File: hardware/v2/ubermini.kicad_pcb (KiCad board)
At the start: 4 copper layers, 76.2 x 63.5 mm, 71 parts, among them J1 USB_OTG, P1 SMA-CONN, P2 sma, P3 sma, P4 uart1, P5 SWD, P6 boot, P7 sma, SW1 SW_PUSH, U1 CC2591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

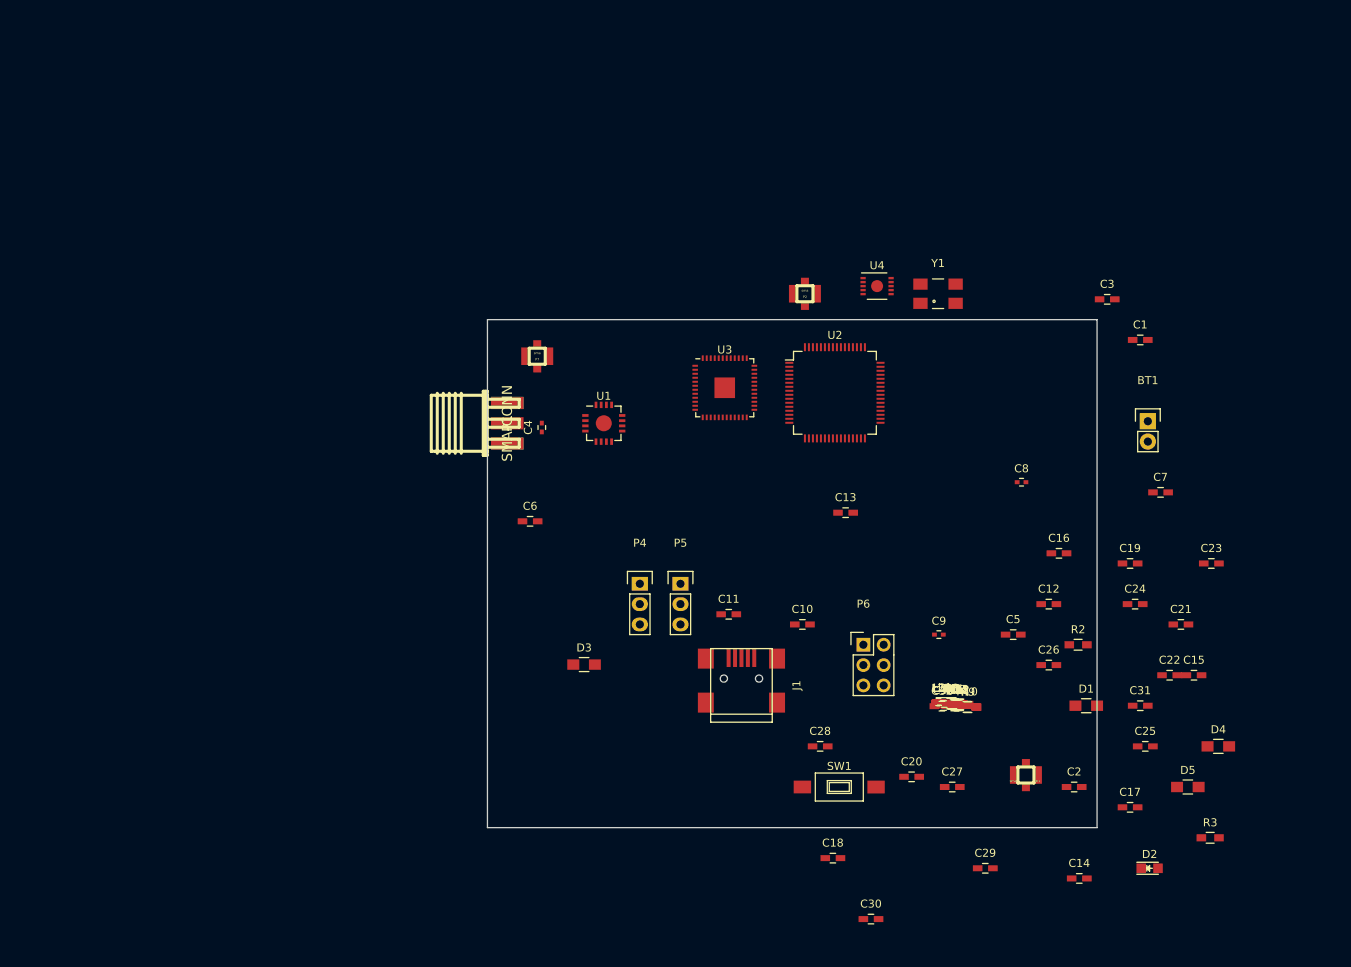
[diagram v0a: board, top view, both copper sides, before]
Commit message: hw v2 add pcb
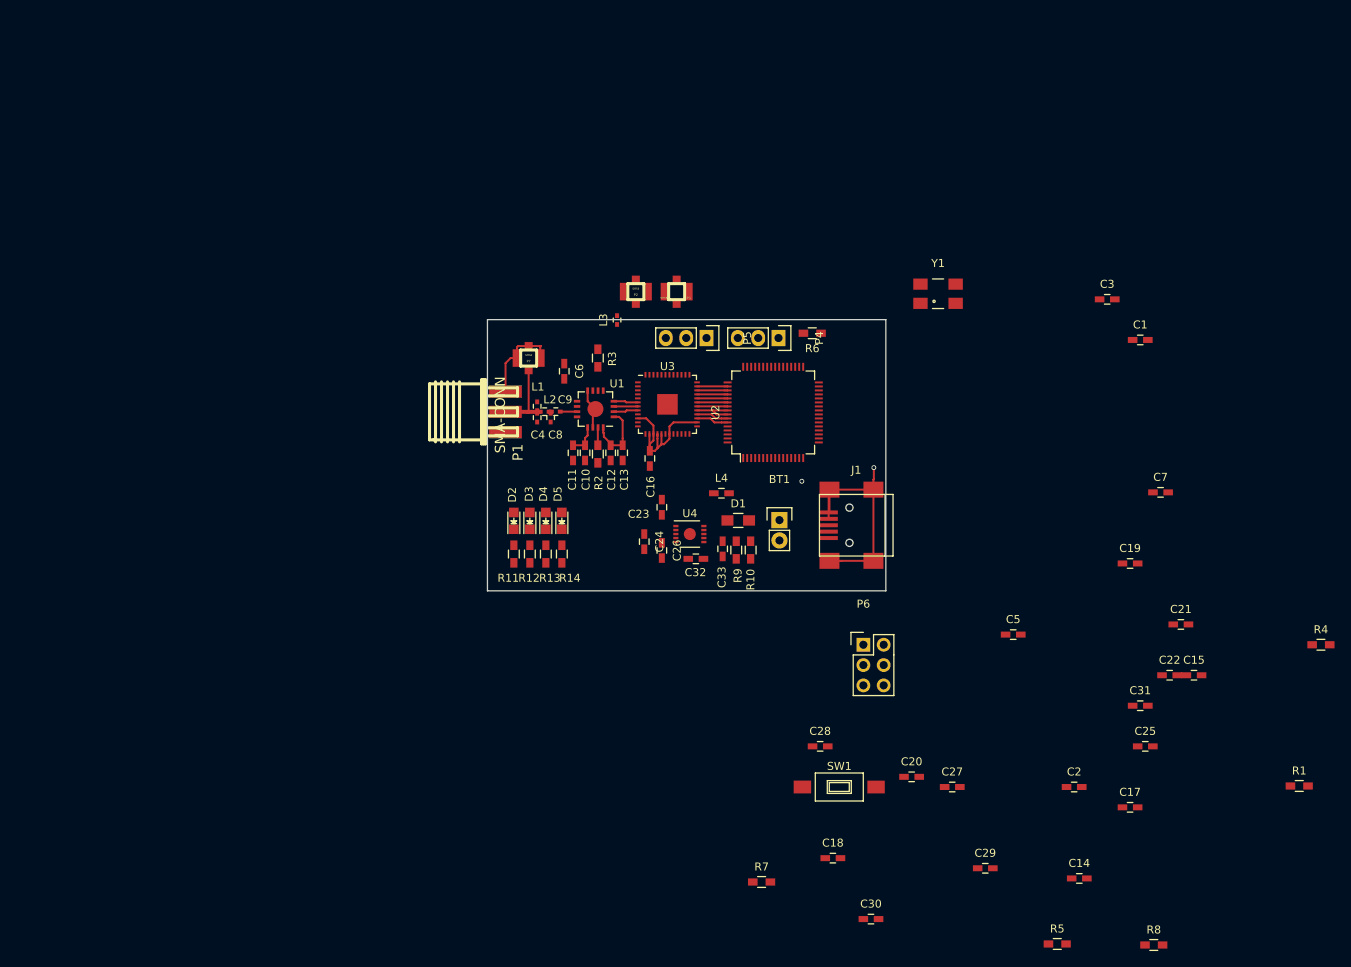
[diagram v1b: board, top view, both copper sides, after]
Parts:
- D3, D4, D5: footprint Resistors_SMD:R_0805_HandSoldering -> LEDs:LED_0805
- moved R3 97.2 mm to (128.1, 81.0), turned to 270 degrees
- moved D2 90.6 mm to (117.6, 101.3), turned to 90 degrees
- moved D4 88.7 mm to (121.6, 101.3), turned to 90 degrees
- moved D5 85.0 mm to (123.6, 101.3), turned to 90 degrees
- moved P3 74.5 mm to (138.0, 72.7)
- moved C23 69.0 mm to (136.1, 99.7), turned to 90 degrees
- moved R2 64.6 mm to (128.1, 93.0), turned to 270 degrees
- moved L3 62.4 mm to (130.5, 76.2), turned to 90 degrees
- moved L1 62.3 mm to (120.5, 87.0), turned to 270 degrees
- moved C24 61.9 mm to (133.9, 104.0), turned to 270 degrees
- moved L2 61.1 mm to (121.5, 87.7)
- moved C8 59.4 mm to (122.2, 88.5), turned to 90 degrees
- moved R11 58.0 mm to (117.6, 105.5), turned to 270 degrees
- moved C12 57.9 mm to (129.7, 92.8), turned to 270 degrees
- moved R12 56.9 mm to (119.6, 105.5), turned to 270 degrees
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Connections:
- U2 pad 50: (no net) -> /GIO6
- U2 pad 51: (no net) -> /SO
- U2 pad 52: (no net) -> /SI
- U2 pad 53: (no net) -> /SCLK
- U2 pad 54: (no net) -> /CSn
- U2 pad 55: (no net) -> /DCLK
- U2 pad 56: (no net) -> /DIO
- U2 pad 57: (no net) -> /DIO
- U2 pad 58: (no net) -> /TX
- U2 pad 59: (no net) -> /RX
- U3 pad 27: (no net) -> /RX
- U3 pad 28: (no net) -> /TX
- U3 pad 29: (no net) -> /DIO
- U3 pad 30: (no net) -> /DCLK
- U3 pad 31: (no net) -> /CSn
- U3 pad 32: (no net) -> /SCLK
- U3 pad 33: (no net) -> /SI
- U3 pad 34: (no net) -> /SO
- U3 pad 35: (no net) -> /GIO6
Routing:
- net GND: track 0.00 -> 55.5 mm, vias 0 -> 2
- net +1V8: track 0.00 -> 19.4 mm
- net +3.3VA: track 0.00 -> 12.4 mm
- net Net-(C4-Pad2): track 0.00 -> 10.4 mm
- net /DIO: track 0.00 -> 5.92 mm
- net /TX: track 0.00 -> 4.03 mm
- net /RX: track 0.00 -> 4.03 mm
- net /SO: track 0.00 -> 3.82 mm
- net /SI: track 0.00 -> 3.82 mm
- net /SCLK: track 0.00 -> 3.82 mm
- net /GIO6: track 0.00 -> 3.82 mm
- net /DCLK: track 0.00 -> 3.82 mm
- net /CSn: track 0.00 -> 3.82 mm
- net Net-(L3-Pad2): track 0.00 -> 3.07 mm
- net Net-(L3-Pad1): track 0.00 -> 3.06 mm
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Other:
- board size 76.2 x 63.5 mm -> 49.8 x 33.9 mm

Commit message: hw patch
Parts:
- moved R8 76.2 mm to (129.5, 120.2), turned to 180 degrees
- moved R1 71.4 mm to (147.9, 112.3)
- moved C18 70.1 mm to (130.6, 78.8), turned to 270 degrees
- moved C19 62.1 mm to (139.2, 78.8), turned to 90 degrees
- moved C1 59.5 mm to (148.1, 114.1), turned to 180 degrees
- moved R5 56.4 mm to (140.6, 120.2), turned to 180 degrees
- moved SW1 51.8 mm to (170.8, 84.4), turned to 90 degrees
- moved R7 49.9 mm to (156.9, 97.3), turned to 90 degrees
- moved Y1 36.2 mm to (134.9, 79.0)
- moved BT1 33.2 mm to (118.1, 106.8), turned to 180 degrees
- moved P6 31.9 mm to (159.0, 85.1)
- moved D2 23.4 mm to (141.0, 101.7)
- moved D3 23.4 mm to (143.0, 101.8)
- moved D4 23.4 mm to (145.0, 101.7)
- moved D5 23.4 mm to (147.0, 101.7)
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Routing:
- net GND: track 55.5 -> 5.30 mm, vias 2 -> 0
- net Net-(C4-Pad2): track 10.4 -> 5.18 mm

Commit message: hw update
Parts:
- C2, C22, C27, C28, C29, C30, C5, R3, R4, R8: moved to B.Cu
- moved C14 84.6 mm to (130.5, 84.2), turned to 180 degrees
- moved R4 84.6 mm to (140.4, 84.2), turned to 180 degrees
- moved C15 80.4 mm to (131.7, 82.9), turned to 180 degrees
- moved C7 75.0 mm to (124.6, 84.5), turned to 270 degrees
- moved C17 72.3 mm to (136.2, 94.5), turned to 270 degrees
- moved C29 65.4 mm to (146.2, 86.8), turned to 270 degrees
- moved C25 63.1 mm to (141.3, 99.0), turned to 270 degrees
- moved C21 62.4 mm to (142.1, 93.8), turned to 270 degrees
- moved C30 62.3 mm to (146.4, 90.8), turned to 90 degrees
- moved C31 61.9 mm to (139.5, 99.0), turned to 270 degrees
- moved C2 61.0 mm to (151.4, 85.5), turned to 180 degrees
- moved C20 57.5 mm to (140.3, 82.6), turned to 180 degrees
- moved C3 56.4 mm to (139.6, 95.0), turned to 90 degrees
- moved C22 55.8 mm to (151.9, 91.6), turned to 180 degrees
- moved C27 54.3 mm to (152.8, 84.0), turned to 180 degrees
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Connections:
- net /ATEST1 renamed /ATEST1_P
- net /ATEST2 renamed /ATEST2_N
- D2 pad 2: (no net) -> /LED1
- D3 pad 2: (no net) -> /LED2
- D4 pad 2: (no net) -> /LED3
- D5 pad 2: (no net) -> /LED4
- U1 pad 7: (no net) -> /HGM
- U2 pad 1: (no net) -> Net-(U2-Pad1)
- U2 pad 10: (no net) -> /LED3
- U2 pad 11: (no net) -> /LED4
- U2 pad 14: (no net) -> Net-(U2-Pad14)
- U2 pad 15: (no net) -> Net-(U2-Pad15)
- U2 pad 16: (no net) -> Net-(U2-Pad16)
- U2 pad 17: (no net) -> Net-(U2-Pad17)
- U2 pad 2: (no net) -> Net-(U2-Pad2)
- U2 pad 20: (no net) -> /SPI1_CS
- U2 pad 21: (no net) -> /SPI1_SCK
- U2 pad 22: (no net) -> /SPI1_MI
- U2 pad 23: (no net) -> /SPI1_MO
- U2 pad 24: (no net) -> Net-(U2-Pad24)
- U2 pad 25: (no net) -> Net-(U2-Pad25)
- U2 pad 26: (no net) -> Net-(U2-Pad26)
- U2 pad 27: (no net) -> Net-(U2-Pad27)
- U2 pad 29: (no net) -> Net-(U2-Pad29)
- U2 pad 3: (no net) -> Net-(U2-Pad3)
- U2 pad 30: (no net) -> Net-(U2-Pad30)
- U2 pad 33: (no net) -> Net-(U2-Pad33)
- U2 pad 34: (no net) -> Net-(U2-Pad34)
- U2 pad 35: (no net) -> Net-(U2-Pad35)
- U2 pad 36: (no net) -> Net-(U2-Pad36)
- U2 pad 37: (no net) -> Net-(U2-Pad37)
- U2 pad 38: (no net) -> Net-(U2-Pad38)
- U2 pad 39: (no net) -> Net-(U2-Pad39)
- U2 pad 4: (no net) -> Net-(U2-Pad4)
- U2 pad 40: (no net) -> Net-(U2-Pad40)
- U2 pad 41: (no net) -> Net-(U2-Pad41)
- U2 pad 6: (no net) -> Net-(U2-Pad6)
- U2 pad 61: (no net) -> /GR
- U2 pad 62: (no net) -> Net-(U2-Pad62)
- U2 pad 8: (no net) -> /LED1
- U2 pad 9: (no net) -> /LED2
- U3 pad 11: (no net) -> Net-(U3-Pad11)
- U3 pad 12: (no net) -> Net-(U3-Pad12)
- U3 pad 13: (no net) -> Net-(U3-Pad13)
- U3 pad 20: (no net) -> /GR
- U3 pad 36: (no net) -> Net-(U3-Pad36)
- U3 pad 37: (no net) -> Net-(U3-Pad37)
- U3 pad 38: (no net) -> Net-(U3-Pad38)
- U3 pad 39: (no net) -> Net-(U3-Pad39)
- U3 pad 40: (no net) -> Net-(U3-Pad40)
- U4 pad 2: (no net) -> Net-(U4-Pad2)
- U4 pad 7: +3.3VA -> Net-(C33-Pad2)
- U4 pad 9: (no net) -> Net-(U4-Pad9)
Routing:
- net GND: track 5.30 -> 227.9 mm, vias 0 -> 17
- net /VBUS: track 0.00 -> 50.1 mm, vias 0 -> 2
- net Net-(R7-Pad2): track 0.00 -> 19.6 mm, vias 0 -> 2
- net /ATEST1_P: track 0.00 -> 18.8 mm, vias 0 -> 2
- net /ATEST2_N: track 0.00 -> 18.7 mm, vias 0 -> 2
- net Net-(R6-Pad2): track 0.00 -> 18.2 mm
- net +1V8: track 19.4 -> 37.3 mm
- net /NRST: track 0.00 -> 17.0 mm, vias 0 -> 2
- net Net-(P6-Pad3): track 0.00 -> 13.9 mm
- net +3.3VA: track 12.4 -> 24.7 mm
- net /GR: track 0.00 -> 11.5 mm, vias 0 -> 2
- net +3V3: track 0.00 -> 10.5 mm, vias 0 -> 2
- net /BOOT0: track 0.00 -> 10.3 mm, vias 0 -> 1
- net Net-(C3-Pad1): track 0.00 -> 10.3 mm
- net Net-(C4-Pad2): track 5.18 -> 15.0 mm
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
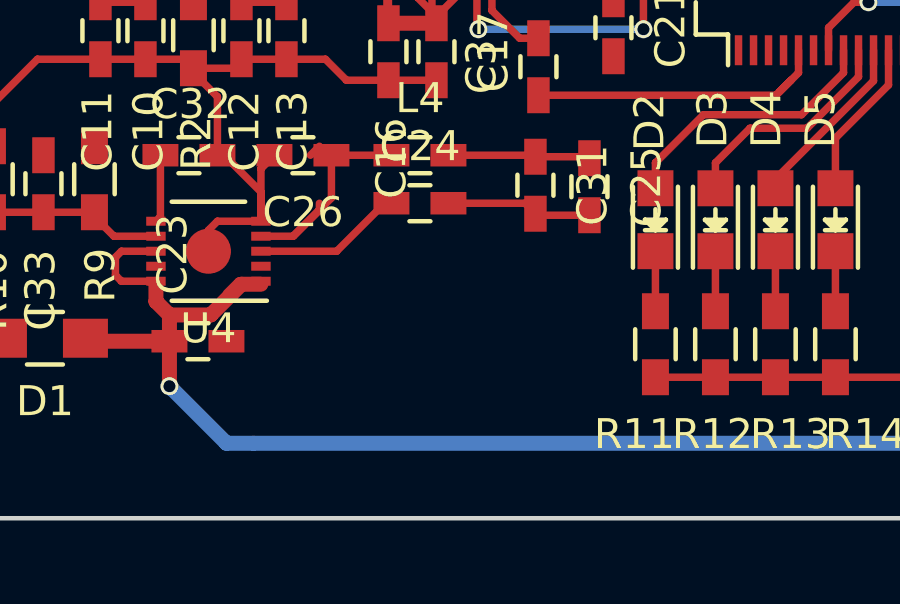
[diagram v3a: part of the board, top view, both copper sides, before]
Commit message: hw: add spi flash
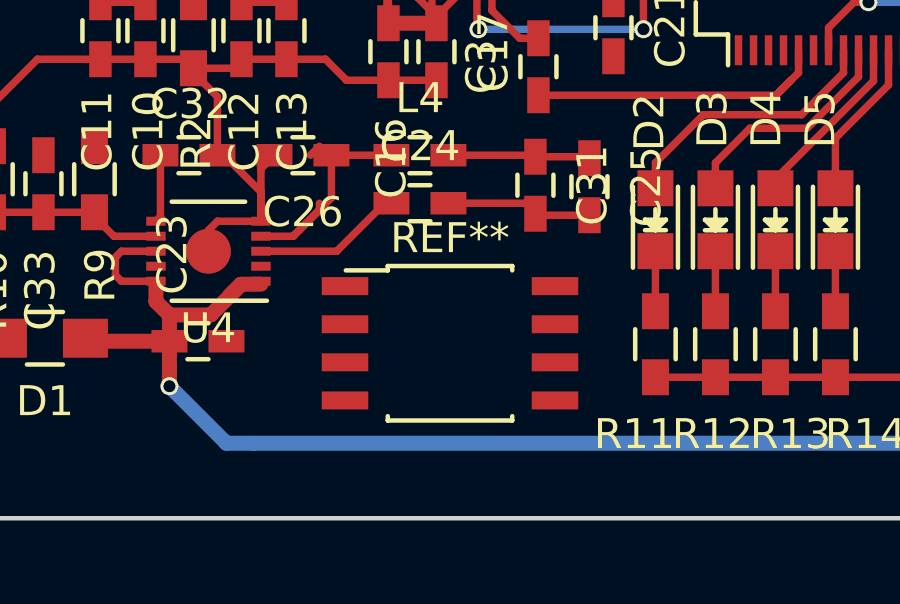
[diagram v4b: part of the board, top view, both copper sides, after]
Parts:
- added REF**: SOIC-8_3.9x4.9mm_Pitch1.27mm, v2:winband_spi_flash, F.Cu at (136.7, 104.2)
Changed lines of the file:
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@@
-(kicad_pcb (version 4) (host pcbnew 4.0.6)
+(kicad_pcb (version 4) (host pcbnew 4.0.4-stable)
   (general
-    (links 206)
-    (no_connects 104)
+    (links 0)
+    (no_connects 56)
     (area 94.670774 63.62619 165.47618 126.047501)
     (thickness 1.6)
@@
     (tracks 658)
     (zones 0)
-    (modules 71)
+    (modules 72)
     (nets 97)
   )
@@
     )
   )
+  (module v2:winband_spi_flash (layer F.Cu)
+    (at 136.652 104.158)
+    (descr "8-Lead Plastic Small Outline (SN) - Narrow, 3.90 mm Body [SOIC] (see Microchip Packaging Specification 00000049BS.pdf)")
+    (tags "SOIC 1.27")
+    (attr smd)
+    (fp_text reference REF** (at 0 -3.39) (layer F.SilkS)
+      (effects (font (size 1 1) (thickness 0.15)))
+    )
+    (fp_text value SOIC-8_3.9x4.9mm_Pitch1.27mm (at 0 3.61) (layer F.Fab)
+      (effects (font (size 1 1) (thickness 0.15)))
+    )
+    (fp_line (start -3.75 -2.64) (end -3.75 2.86) (layer F.CrtYd) (width 0.05))
+    (fp_line (start 3.75 -2.64) (end 3.75 2.86) (layer F.CrtYd) (width 0.05))
+    (fp_line (start -3.75 -2.64) (end 3.75 -2.64) (layer F.CrtYd) (width 0.05))
+    (fp_line (start -3.75 2.86) (end 3.75 2.86) (layer F.CrtYd) (width 0.05))
+    (fp_line (start -2.075 -2.465) (end -2.075 -2.32) (layer F.SilkS) (width 0.15))
+    (fp_line (start 2.075 -2.465) (end 2.075 -2.32) (layer F.SilkS) (width 0.15))
+    (fp_line (start 2.075 2.685) (end 2.075 2.54) (layer F.SilkS) (width 0.15))
+    (fp_line (start -2.075 2.685) (end -2.075 2.54) (layer F.SilkS) (width 0.15))
+    (fp_line (start -2.075 -2.465) (end 2.075 -2.465) (layer F.SilkS) (width 0.15))
+    (fp_line (start -2.075 2.685) (end 2.075 2.685) (layer F.SilkS) (width 0.15))
+    (fp_line (start -2.075 -2.32) (end -3.475 -2.32) (layer F.SilkS) (width 0.15))
+    (pad 1 smd rect (at -3.5 -1.795) (size 1.55 0.6) (layers F.Cu F.Paste F.Mask))
+    (pad 2 smd rect (at -3.5 -0.525) (size 1.55 0.6) (layers F.Cu F.Paste F.Mask))
+    (pad 3 smd rect (at -3.5 0.745) (size 1.55 0.6) (layers F.Cu F.Paste F.Mask))
+    (pad 4 smd rect (at -3.5 2.015) (size 1.55 0.6) (layers F.Cu F.Paste F.Mask))
+    (pad 5 smd rect (at 3.5 2.015) (size 1.55 0.6) (layers F.Cu F.Paste F.Mask))
+    (pad 6 smd rect (at 3.5 0.745) (size 1.55 0.6) (layers F.Cu F.Paste F.Mask))
+    (pad 7 smd rect (at 3.5 -0.525) (size 1.55 0.6) (layers F.Cu F.Paste F.Mask))
+    (pad 8 smd rect (at 3.5 -1.795) (size 1.55 0.6) (layers F.Cu F.Paste F.Mask))
+    (model Housings_SOIC.3dshapes/SOIC-8_3.9x4.9mm_Pitch1.27mm.wrl
+      (at (xyz 0 0 0))
+      (scale (xyz 1.2 1 1))
+      (rotate (xyz 0 0 0))
+    )
+  )
   (target plus (at 114.3 110) (size 5) (width 0.15) (layer Edge.Cuts))
   (dimension 34.036059 (width 0.3) (layer Eco1.User)
@@
   (segment (start 133.2 95.5) (end 134.6 95.5) (width 0.25) (layer F.Cu) (net 2))
   (segment (start 131.2 94.8) (end 132.5 94.8) (width 0.25) (layer F.Cu) (net 2))
-  (segment (start 132 98) (end 132.3 97.7) (width 0.25) (layer F.Cu) (net 2))
   (segment (start 120.5135 87.481) (end 120.5135 86.931) (width 0.25) (layer F.Cu) (net 2))
   (segment (start 120.5 84.1) (end 121 83.6) (width 0.25) (layer F.Cu) (net 2))
@@
   (segment (start 146.77 84.47) (end 147 84.7) (width 0.25) (layer F.Cu) (net 8))
   (via (at 147 84.7) (size 0.6) (drill 0.4) (layers F.Cu B.Cu) (net 8))
+  (segment (start 132 98) (end 132.3 97.7) (width 0.25) (layer F.Cu) (net 9))
   (segment (start 124.6 85.5) (end 124.6 87.8) (width 0.25) (layer F.Cu) (net 9))
   (segment (start 124.6 87.8) (end 124.85 88.05) (width 0.25) (layer F.Cu) (net 9))

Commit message: hw update
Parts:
- removed L3: DNP, Capacitors_SMD:C_0402
- removed REF**: SOIC-8_3.9x4.9mm_Pitch1.27mm, v2:winband_spi_flash
- added D6: LED, LEDs:LED_0805, F.Cu at (143.1, 115.4)
- added R15: 10k, Resistors_SMD:R_0603_HandSoldering, F.Cu at (136.3, 118.0)
- added U5: M25PX32-VMW, v2:winband_spi_flash, F.Cu at (136.6, 104.3)
- C28: moved to F.Cu
- moved R4 2.11 mm to (140.2, 82.1)
- moved C28 0.70 mm to (153.0, 98.3)
- moved C22 0.14 mm to (152.1, 91.5)
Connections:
- U2 pad 1: Net-(U2-Pad1) -> (no net)
- U2 pad 14: Net-(U2-Pad14) -> (no net)
- U2 pad 15: Net-(U2-Pad15) -> (no net)
- U2 pad 16: Net-(U2-Pad16) -> (no net)
- U2 pad 17: Net-(U2-Pad17) -> (no net)
- U2 pad 2: Net-(U2-Pad2) -> (no net)
- U2 pad 20: /SPI1_CS -> (no net)
- U2 pad 24: Net-(U2-Pad24) -> (no net)
- U2 pad 25: Net-(U2-Pad25) -> (no net)
- U2 pad 26: Net-(U2-Pad26) -> (no net)
- U2 pad 27: Net-(U2-Pad27) -> (no net)
- U2 pad 29: Net-(U2-Pad29) -> (no net)
- U2 pad 3: Net-(U2-Pad3) -> /EN
- U2 pad 30: Net-(U2-Pad30) -> (no net)
- U2 pad 33: Net-(U2-Pad33) -> (no net)
- U2 pad 34: Net-(U2-Pad34) -> (no net)
- U2 pad 35: Net-(U2-Pad35) -> (no net)
- U2 pad 36: Net-(U2-Pad36) -> (no net)
- U2 pad 37: Net-(U2-Pad37) -> (no net)
- U2 pad 38: Net-(U2-Pad38) -> (no net)
- U2 pad 39: Net-(U2-Pad39) -> (no net)
- U2 pad 4: Net-(U2-Pad4) -> /HGM
- U2 pad 40: Net-(U2-Pad40) -> (no net)
- U2 pad 41: Net-(U2-Pad41) -> (no net)
- U2 pad 6: Net-(U2-Pad6) -> (no net)
- U2 pad 62: Net-(U2-Pad62) -> (no net)
- U3 pad 11: Net-(U3-Pad11) -> (no net)
- U3 pad 12: Net-(U3-Pad12) -> (no net)
- U3 pad 13: Net-(U3-Pad13) -> (no net)
- U3 pad 36: Net-(U3-Pad36) -> (no net)
- U3 pad 37: Net-(U3-Pad37) -> (no net)
- U3 pad 38: Net-(U3-Pad38) -> (no net)
- U3 pad 39: Net-(U3-Pad39) -> (no net)
- U3 pad 40: Net-(U3-Pad40) -> (no net)
- U4 pad 2: Net-(U4-Pad2) -> (no net)
- U4 pad 9: Net-(U4-Pad9) -> (no net)
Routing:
- net GND: track 227.5 -> 441.9 mm, vias 17 -> 40
- net +3V3: track 10.5 -> 72.5 mm, vias 2 -> 7
- net +3.3VA: track 25.1 -> 73.7 mm, vias 0 -> 6
- net /HGM: track 0.00 -> 36.1 mm, vias 0 -> 2
- net +1V8: track 37.3 -> 71.1 mm, vias 0 -> 6
- net /EN: track 4.06 -> 31.6 mm, vias 1 -> 2
- net /NRST: track 17.0 -> 20.7 mm
- net Net-(R4-Pad2): track 2.54 -> 6.18 mm
